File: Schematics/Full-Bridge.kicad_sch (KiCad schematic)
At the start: 0 parts

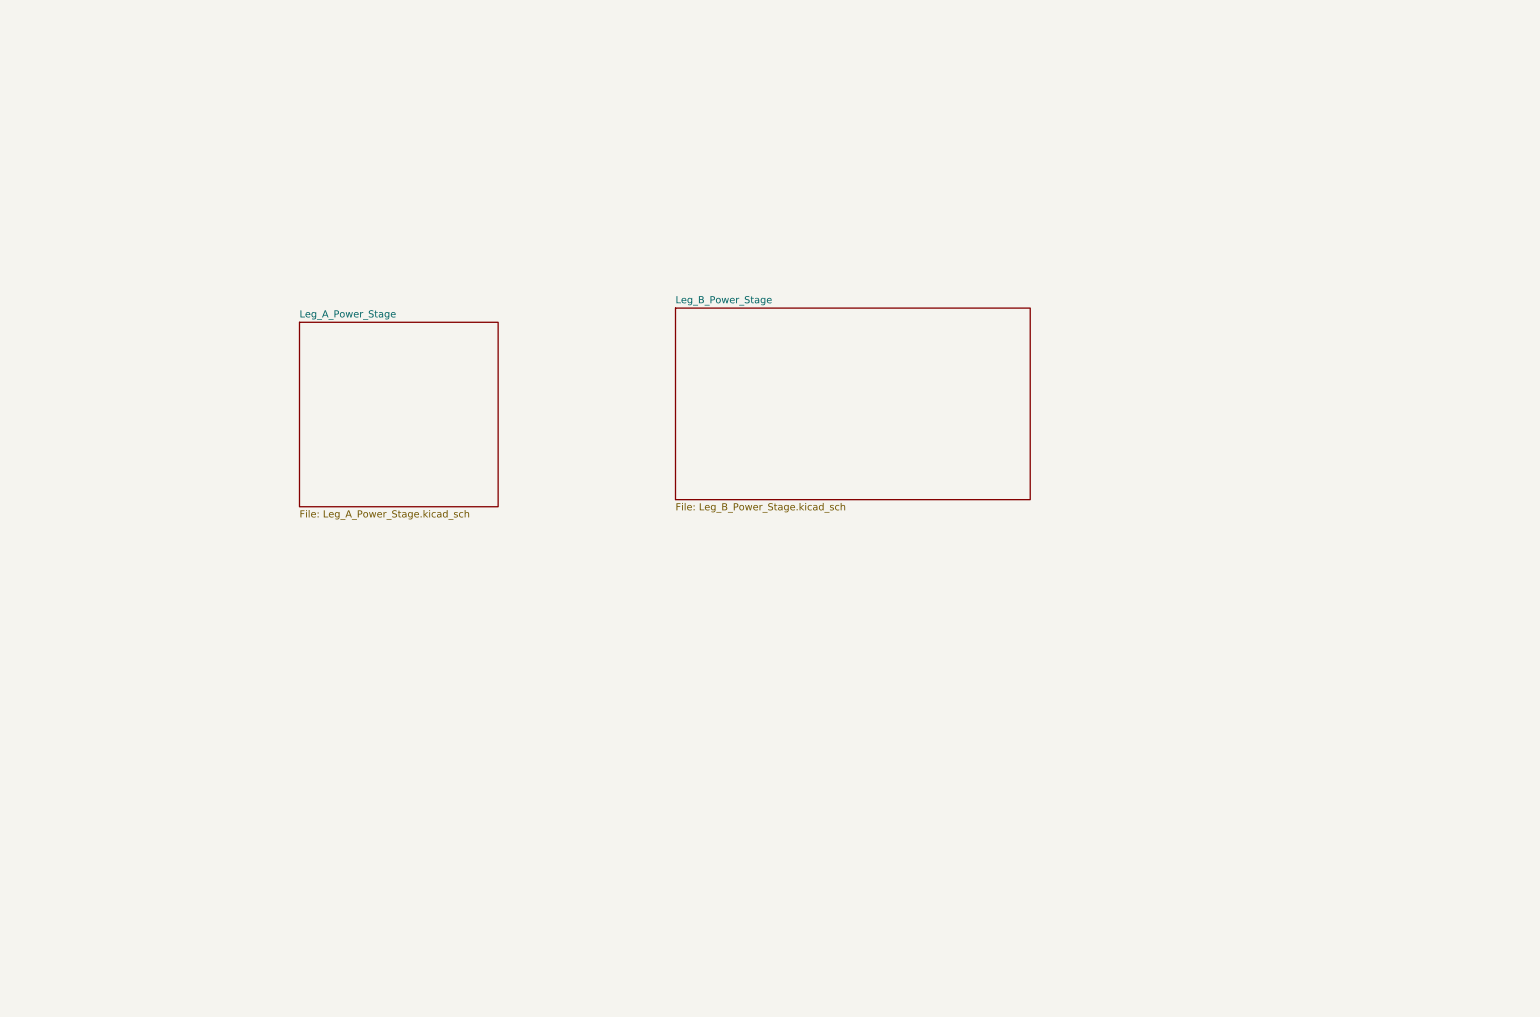
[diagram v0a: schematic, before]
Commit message: [WIP - SIC Inverter]
- Added 3d models for 3 parts
- Added 3 new footprints for the 3 added parts
- Changed footprint 23AH8785 and 86 Black and Red
- Finished WIP with EMI, Input Protection, and Precharge
- Added datasheet
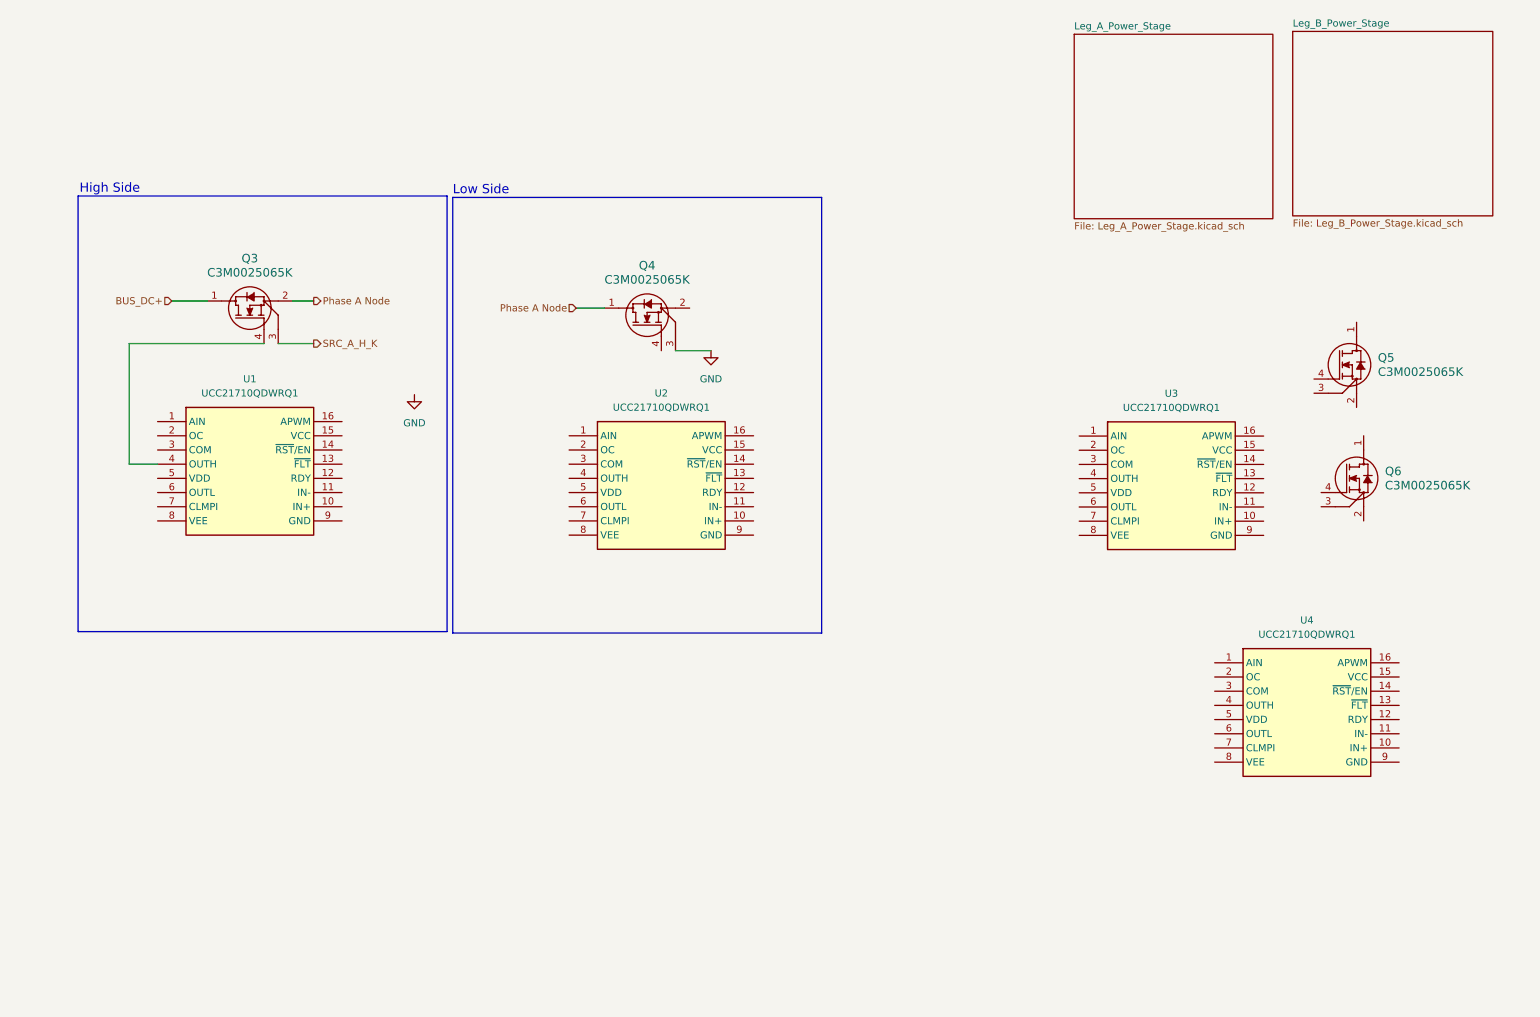
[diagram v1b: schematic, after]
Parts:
- added Q3, Q4, Q5, Q6: C3M0025065K, SiC_Inverter:C3M0025065K, symbol SiC_Inverter:C3M0025065K
- added U1, U2, U3, U4: UCC21710QDWRQ1, SiC_Inverter:UCC21710QDWRQ1, symbol SiC_Inverter:UCC21710QDWRQ1
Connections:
- new net: Q3.4, U1.4 (OUTH)
- new net BUS_DC+: Q3.1
- new net GND: Q4.3
- new net Phase A Node: Q3.2, Q4.1
- new net SRC_A_H_K: Q3.3
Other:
- note added: "High Side"
- note added: "Low Side"

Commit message: [WIP Full Bridge Leg A High Side]
- Changed Footprint for Black and Red connectors to THP but no Pin
  number
- Changed DC Link cap sub sheet to have a cleaner look
- Change footprint in 1206 reister to head solder pads
- WIP Full Bridge Leg A High Side
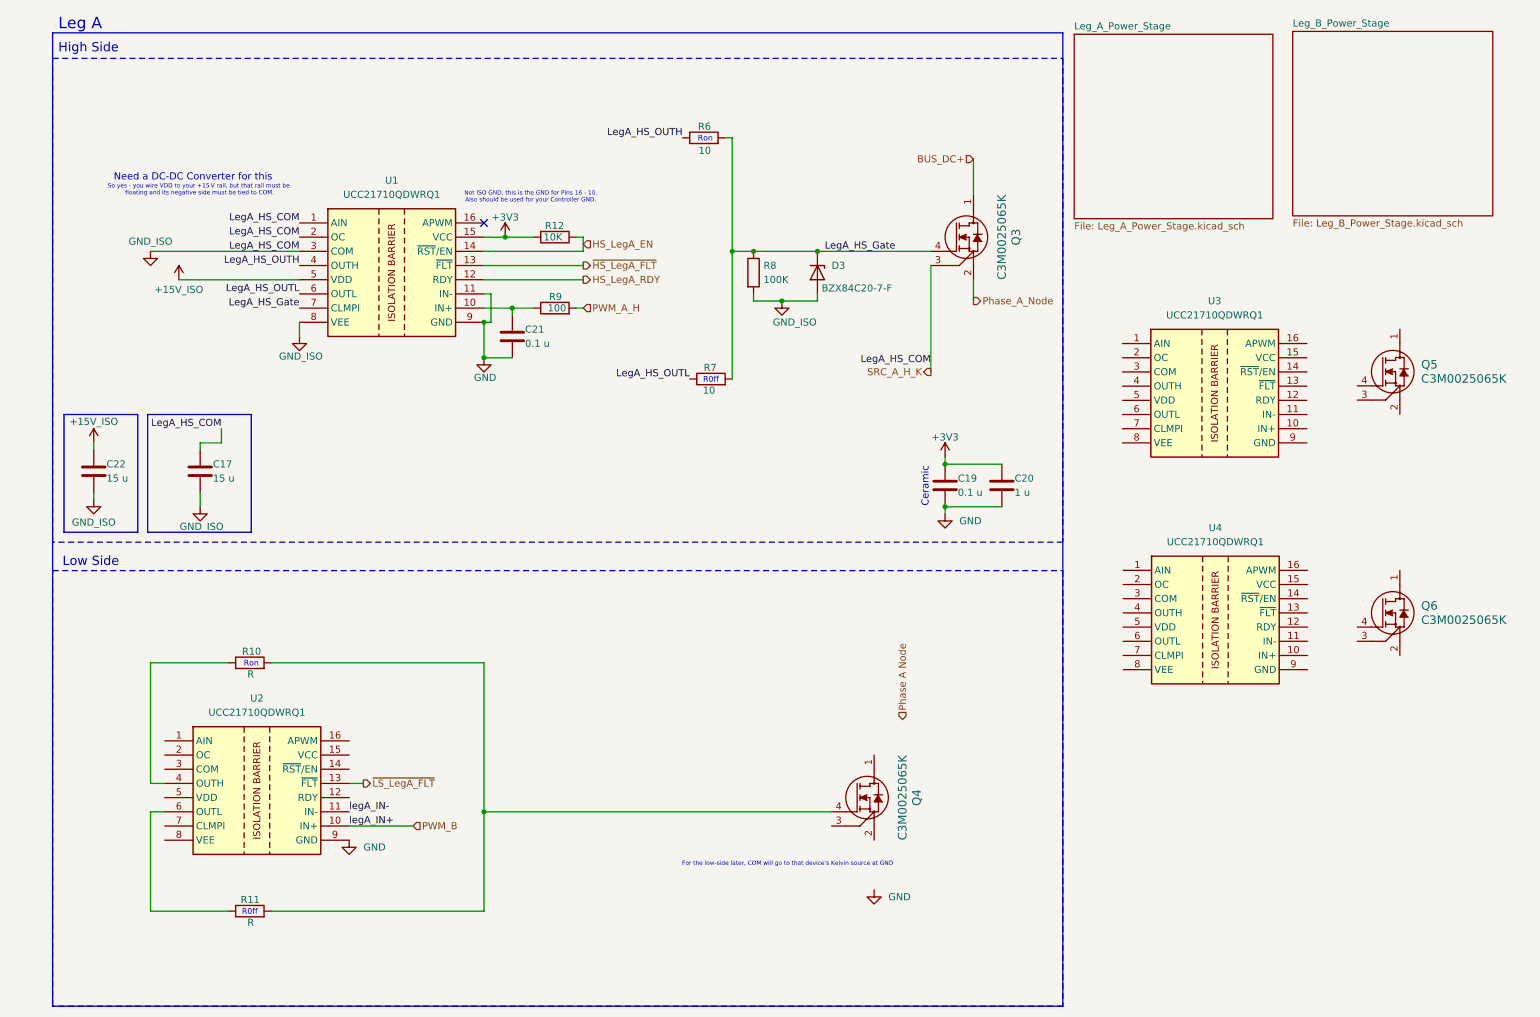
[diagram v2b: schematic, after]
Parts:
- added C17, C22: 15 u, symbol Device:C
- added C19, C21: 0.1 u, symbol Device:C
- added C20: 1 u, symbol Device:C
- added D3: BZX84C20-7-F, Package_TO_SOT_SMD:SOT-23-3, symbol SiC_Inverter:BZX84C20-7-F
- added R10, R11: R, Resistor_SMD:R_1206_3216Metric_Pad1.30x1.75mm_HandSolder, symbol Device:R
- added R12: 10K, Resistor_SMD:R_1206_3216Metric_Pad1.30x1.75mm_HandSolder, symbol Device:R
- added R6, R7: 10, Resistor_SMD:R_1206_3216Metric_Pad1.30x1.75mm_HandSolder, symbol Device:R
- added R8: 100K, Resistor_SMD:R_1206_3216Metric_Pad1.30x1.75mm_HandSolder, symbol Device:R
- added R9: 100, Resistor_SMD:R_1206_3216Metric_Pad1.30x1.75mm_HandSolder, symbol Device:R
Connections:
- net SRC_A_H_K is gone; now on net GND_ISO: Q3.3
- net GND: now also U1.11 (IN-), U1.9 (GND), U2.9 (GND), C19.2, C20.2, C21.2; no longer Q4.3
- net Phase A Node: no longer Q3.2, Q4.1
- net at Q4.4: now also R10.2, R11.2
- net PWM_B: now reaches U2.10 (IN+)
- net legA_IN-: now reaches U2.11 (IN-)
- net ~{LS_LegA_FLT}: now reaches U2.13 (~{FLT})
- net at U2.4 (OUTH): now also R10.1
- net at U2.6 (OUTL): now also R11.1
- net LegA_HS_Gate: now reaches Q3.4
- net LegA_HS_Gate: now also U1.7 (CLMPI), D3.1 (K), R6.2, R7.2, R8.1; no longer U1.4 (OUTH)
- net GND_ISO: now reaches U1.1 (AIN)
- net GND_ISO: now also U1.2 (OC), U1.3 (COM), U1.8 (VEE), C17.1, C17.2, C22.2, D3.2 (A), R8.2
- net at U1.10 (IN+): now also C21.1, R9.1
- net HS_LegA_RDY: now reaches U1.12 (RDY)
- net ~{HS_LegA_FLT}: now reaches U1.13 (~{FLT})
- net HS_LegA_EN: now reaches U1.14 (~{RST}/EN)
- net HS_LegA_EN: now also R12.1
- net +3V3: now reaches U1.15 (VCC)
- net +3V3: now also C19.1, C20.1, R12.2
- net +15V_ISO: now reaches U1.5 (VDD)
- net +15V_ISO: now also C22.1
- net LegA_HS_OUTL: now reaches U1.6 (OUTL)
- net LegA_HS_OUTL: now also R7.1
- new net LegA_HS_OUTH: R6.1, U1.4 (OUTH)
- new net PWM_A_H: R9.2
- new net Phase_A_Node: Q3.2
- no-connect marks 0 -> 1
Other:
- note added: "Ceramic"
- note added: "For the low‑side later, COM will go to that device's Kelvin source at GND"
- note added: "Leg A"
- note added: "Need a DC-DC Converter for this"
- note added: "Not ISO GND, this is the GND for Pins 16 - 10. Also should be used for your Controller GND."
- note added: "R0ff"
- note added: "Ron"
- note added: "So yes - you wire VDD to your +15 V rail, but that rail must be floating and its negative side must be tied to COM."
- moved on the sheet: Q3, Q4, Q5, Q6

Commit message: [LEG A WIP]
- moved circuits in Leg A HS and LS
- Completed 90% of HS and LS for LEG A
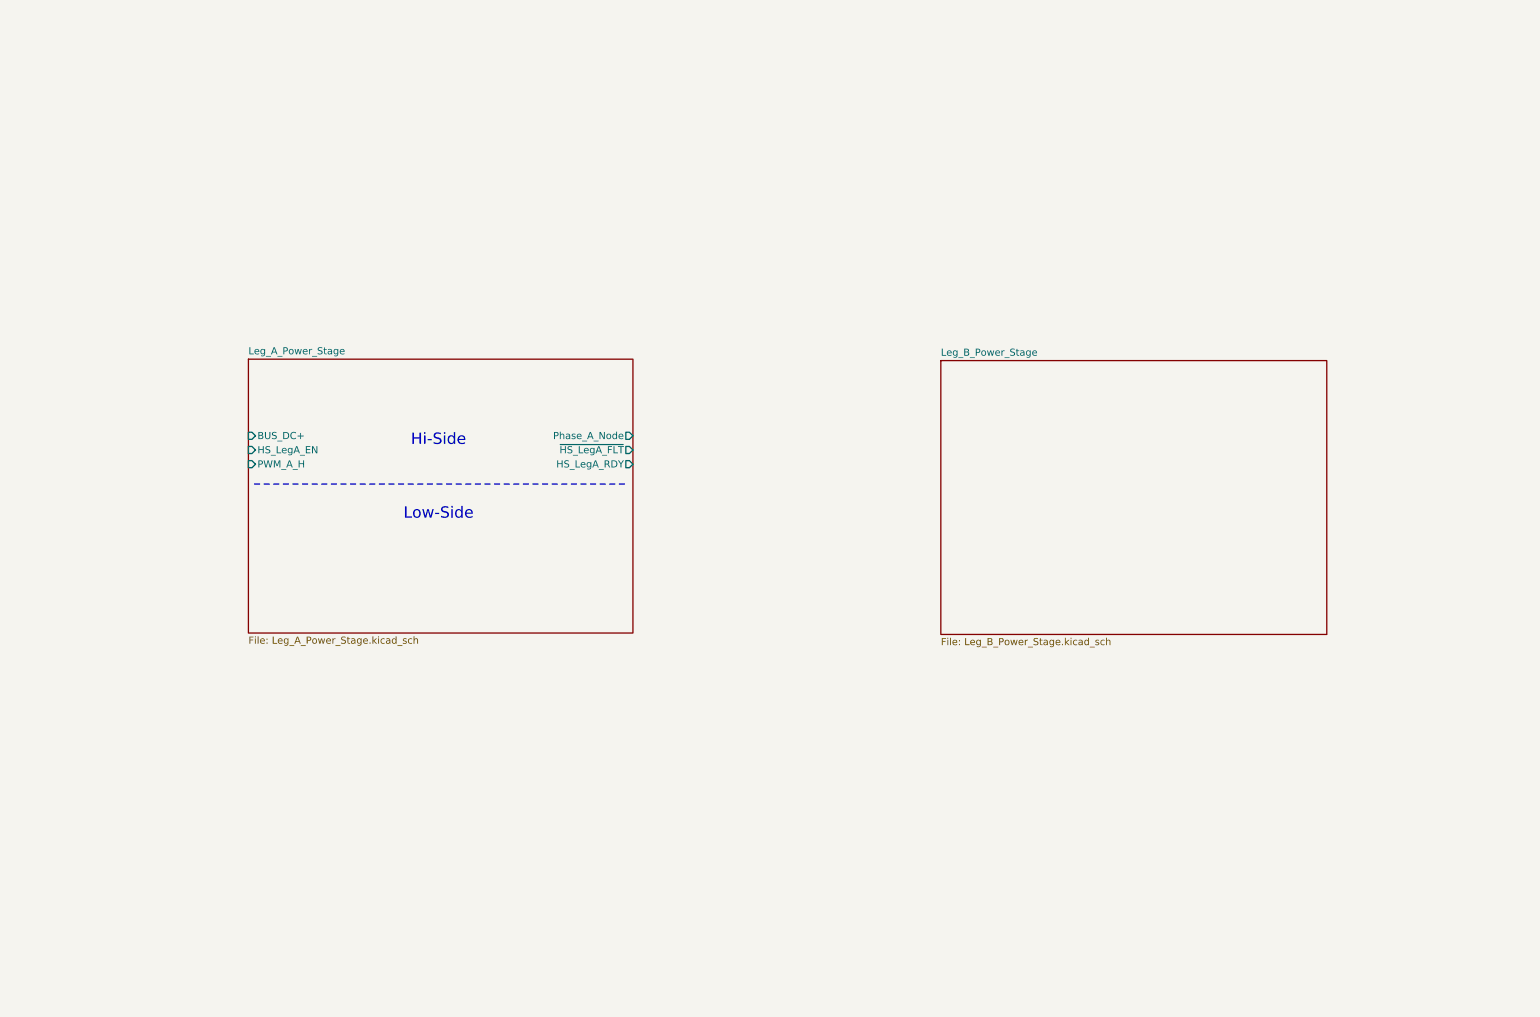
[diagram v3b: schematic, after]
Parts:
- removed C17, C22: 15 u, symbol Device:C
- removed C19, C21: 0.1 u, symbol Device:C
- removed C20: 1 u, symbol Device:C
- removed D3: BZX84C20-7-F, Package_TO_SOT_SMD:SOT-23-3, symbol SiC_Inverter:BZX84C20-7-F
- removed Q3, Q4, Q5, Q6: C3M0025065K, SiC_Inverter:C3M0025065K, symbol SiC_Inverter:C3M0025065K
- removed R10, R11: R, Resistor_SMD:R_1206_3216Metric_Pad1.30x1.75mm_HandSolder, symbol Device:R
- removed R12: 10K, Resistor_SMD:R_1206_3216Metric_Pad1.30x1.75mm_HandSolder, symbol Device:R
- removed R6, R7: 10, Resistor_SMD:R_1206_3216Metric_Pad1.30x1.75mm_HandSolder, symbol Device:R
- removed R8: 100K, Resistor_SMD:R_1206_3216Metric_Pad1.30x1.75mm_HandSolder, symbol Device:R
- removed R9: 100, Resistor_SMD:R_1206_3216Metric_Pad1.30x1.75mm_HandSolder, symbol Device:R
- removed U1, U2, U3, U4: UCC21710QDWRQ1, SiC_Inverter:UCC21710QDWRQ1, symbol SiC_Inverter:UCC21710QDWRQ1
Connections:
- no-connect marks 1 -> 0
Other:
- sheet Leg_A_Power_Stage ports: added BUS_DC+, HS_LegA_EN, HS_LegA_RDY, PWM_A_H, Phase_A_Node, ~{HS_LegA_FLT}; removed none
- note added: "Hi-Side"
- note added: "Low-Side"
- note removed: "Ceramic"
- note removed: "For the low‑side later, COM will go to that device's Kelvin source at GND"
- note removed: "High Side"
- note removed: "Leg A"
- note removed: "Low Side"
- note removed: "Need a DC-DC Converter for this"
- note removed: "Not ISO GND, this is the GND for Pins 16 - 10. Also should be used for your Controller GND."
- note removed: "R0ff"
- note removed: "Ron"
- note removed: "So yes - you wire VDD to your +15 V rail, but that rail must be floating and its negative side must be tied to COM."
